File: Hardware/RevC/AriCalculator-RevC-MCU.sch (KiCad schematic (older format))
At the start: 13 parts, among them CON1 BDM, CON2 SPI, IC1 MC9S12G

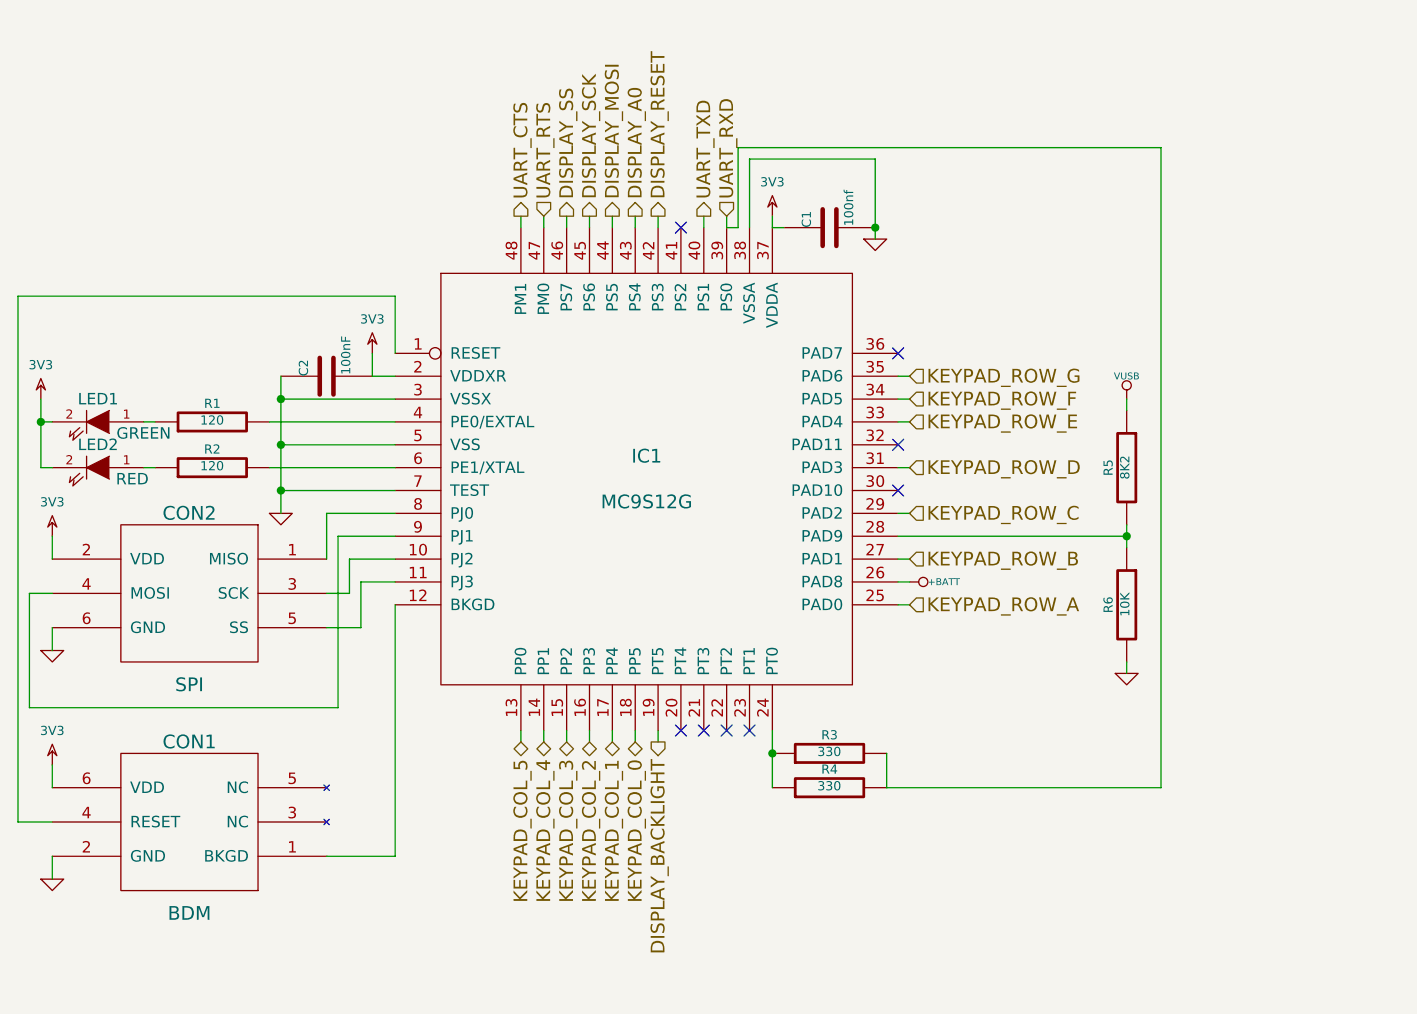
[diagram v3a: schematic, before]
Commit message: started RevC layout
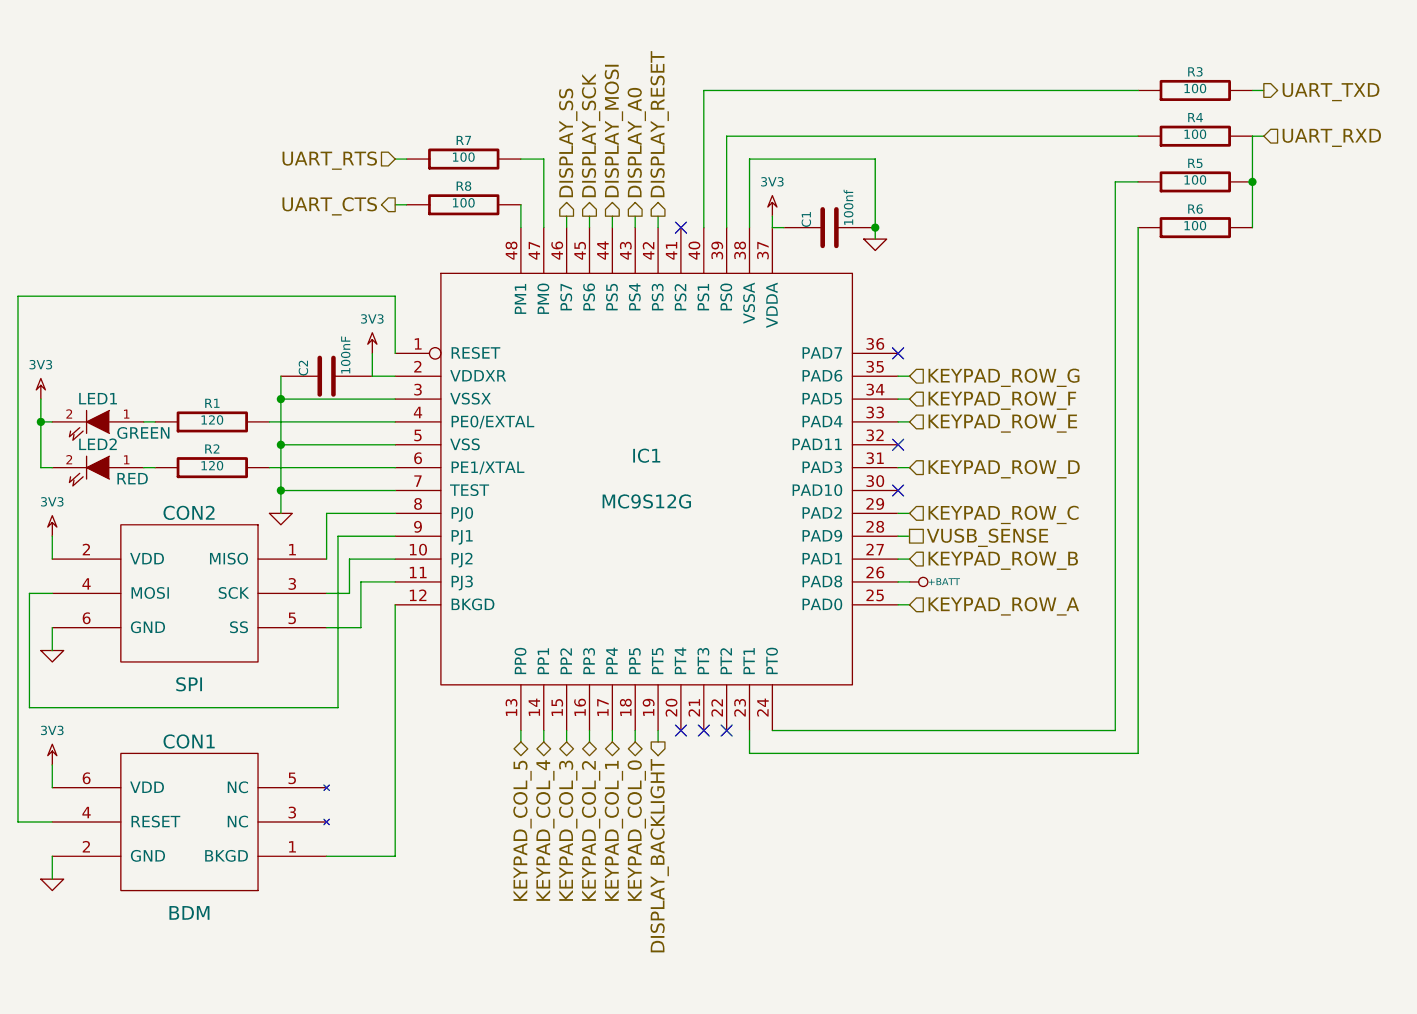
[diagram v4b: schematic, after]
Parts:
- added R7, R8: 100, ~, symbol R
- R3, R4: value 330 -> 100
- R5: value 8K2 -> 100
- R6: value 10K -> 100
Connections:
- net GND: no longer R6.2
- net UART_CTS: now also R8.1; no longer IC1.48 (PM1)
- net UART_RTS: now also R7.1; no longer IC1.47 (PM0)
- net UART_RXD: now also R5.2, R6.2; no longer IC1.39 (PS0), R3.2
- net UART_TXD: now also R3.2; no longer IC1.40 (PS1)
- net at IC1.23 (PT1): now also R6.1
- net VUSB: no longer names the net of R5.1
- net VUSB: now also IC1.24 (PT0)
- new net: IC1.39 (PS0), R4.1
- new net: IC1.40 (PS1), R3.1
- new net: IC1.47 (PM0), R7.2
- new net: IC1.48 (PM1), R8.2
- new net VUSB_SENSE: IC1.28 (PAD9)
- no-connect marks 8 -> 7
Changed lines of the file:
@@
 $EndComp
 $Comp
-L GND #PWR024
+L GND #PWR020
 U 1 1 544FF350
 P 4900 1400
-F 0 "#PWR024" H 4900 1400 30  0001 C CNN
+F 0 "#PWR020" H 4900 1400 30  0001 C CNN
 F 1 "GND" H 4900 1330 30  0001 C CNN
 F 2 "" H 4900 1400 60  0000 C CNN
@@
 $EndComp
 $Comp
-L GND #PWR025
+L GND #PWR021
 U 1 1 544FF410
 P 2300 2600
-F 0 "#PWR025" H 2300 2600 30  0001 C CNN
+F 0 "#PWR021" H 2300 2600 30  0001 C CNN
 F 1 "GND" H 2300 2530 30  0001 C CNN
 F 2 "" H 2300 2600 60  0000 C CNN
@@
 $EndComp
 $Comp
-L GND #PWR026
+L GND #PWR022
 U 1 1 544FF5A5
 P 1300 4200
-F 0 "#PWR026" H 1300 4200 30  0001 C CNN
+F 0 "#PWR022" H 1300 4200 30  0001 C CNN
 F 1 "GND" H 1300 4130 30  0001 C CNN
 F 2 "" H 1300 4200 60  0000 C CNN
@@
 $EndComp
 $Comp
-L GND #PWR027
+L GND #PWR023
 U 1 1 544FF75E
 P 1300 3200
-F 0 "#PWR027" H 1300 3200 30  0001 C CNN
+F 0 "#PWR023" H 1300 3200 30  0001 C CNN
 F 1 "GND" H 1300 3130 30  0001 C CNN
 F 2 "" H 1300 3200 60  0000 C CNN
@@
 	1    0    0    -1
 $EndComp
-$Comp
-L VUSB #PWR028
-U 1 1 54500312
-P 6000 2100
-F 0 "#PWR028" H 6000 2050 20  0001 C CNN
-F 1 "VUSB" H 6000 2200 30  0000 C CNN
-F 2 "" H 6000 2100 60  0000 C CNN
-F 3 "" H 6000 2100 60  0000 C CNN
-	1    6000 2100
-	1    0    0    -1
-$EndComp
-$Comp
-L R R5
-U 1 1 54500321
-P 6000 2400
-F 0 "R5" V 6080 2400 40  0000 C CNN
-F 1 "8K2" V 6007 2401 40  0000 C CNN
-F 2 "~" V 5930 2400 30  0000 C CNN
-F 3 "~" H 6000 2400 30  0000 C CNN
-	1    6000 2400
-	-1   0    0    -1
-$EndComp
-$Comp
-L R R6
-U 1 1 54500330
-P 6000 3000
-F 0 "R6" V 6080 3000 40  0000 C CNN
-F 1 "10K" V 6007 3001 40  0000 C CNN
-F 2 "~" V 5930 3000 30  0000 C CNN
-F 3 "~" H 6000 3000 30  0000 C CNN
-	1    6000 3000
-	-1   0    0    -1
-$EndComp
-$Comp
-L GND #PWR029
-U 1 1 5450033F
-P 6000 3300
-F 0 "#PWR029" H 6000 3300 30  0001 C CNN
-F 1 "GND" H 6000 3230 30  0001 C CNN
-F 2 "" H 6000 3300 60  0000 C CNN
-F 3 "" H 6000 3300 60  0000 C CNN
-	1    6000 3300
-	1    0    0    -1
-$EndComp
-$Comp
-L R R3
-U 1 1 5450048A
-P 4700 3650
-F 0 "R3" V 4780 3650 40  0000 C CNN
-F 1 "330" V 4707 3651 40  0000 C CNN
-F 2 "~" V 4630 3650 30  0000 C CNN
-F 3 "~" H 4700 3650 30  0000 C CNN
-	1    4700 3650
-	0    -1   -1   0
-$EndComp
-$Comp
-L R R4
-U 1 1 54500499
-P 4700 3800
-F 0 "R4" V 4780 3800 40  0000 C CNN
-F 1 "330" V 4707 3801 40  0000 C CNN
-F 2 "~" V 4630 3800 30  0000 C CNN
-F 3 "~" H 4700 3800 30  0000 C CNN
-	1    4700 3800
-	0    -1   -1   0
-$EndComp
 Text HLabel 3950 3600 3    60   Output ~ 0
 DISPLAY_BACKLIGHT
@@
 Connection ~ 1250 2200
 Wire Wire Line
-	6000 2100 6000 2150
-Wire Wire Line
-	6000 2650 6000 2750
-Connection ~ 6000 2700
-Wire Wire Line
-	6000 3250 6000 3300
-Wire Wire Line
-	4450 3550 4450 3800
-Connection ~ 4450 3650
-Wire Wire Line
-	4950 3650 4950 3800
-Wire Wire Line
-	4950 3800 6150 3800
-Wire Wire Line
-	6150 3800 6150 1000
-Wire Wire Line
 	3950 3550 3950 3600
-NoConn ~ 4350 3550
 NoConn ~ 4250 3550
 NoConn ~ 4150 3550
@@
 KEYPAD_ROW_F
 $Comp
-L +BATT #PWR030
+L +BATT #PWR024
 U 1 1 544FFB66
 P 5050 2900
-F 0 "#PWR030" H 5050 2850 20  0001 C CNN
+F 0 "#PWR024" H 5050 2850 20  0001 C CNN
 F 1 "+BATT" V 5050 3050 30  0000 C CNN
 F 2 "" H 5050 2900 60  0000 C CNN
@@
 Wire Wire Line
 	5000 2000 5050 2000
-Text HLabel 3350 1300 1    60   Output ~ 0
+Text HLabel 2800 1250 0    60   Output ~ 0
 UART_CTS
-Text HLabel 3450 1300 1    60   Input ~ 0
+Text HLabel 2800 1050 0    60   Input ~ 0
 UART_RTS
-Text HLabel 4150 1300 1    60   Output ~ 0
+Text HLabel 6600 750  2    60   Output ~ 0
 UART_TXD
-Text HLabel 4250 1300 1    60   Input ~ 0
+Text HLabel 6600 950  2    60   Input ~ 0
 UART_RXD
 Text HLabel 3550 1300 1    60   Output ~ 0
@@
 Connection ~ 4900 1350
 Wire Wire Line
-	4150 1300 4150 1350
-Wire Wire Line
 	3950 1300 3950 1350
 Wire Wire Line
@@
 Wire Wire Line
 	3550 1300 3550 1350
-Wire Wire Line
-	3450 1300 3450 1350
-Wire Wire Line
-	3350 1300 3350 1350
-Wire Wire Line
-	4250 1300 4250 1350
-Wire Wire Line
-	4250 1350 4300 1350
-Wire Wire Line
-	4300 1350 4300 1000
-Wire Wire Line
-	4300 1000 6150 1000
 $Comp
 L 3V3 #PWR32
@@
 Wire Wire Line
 	5050 2900 5000 2900
-Wire Wire Line
-	5000 2700 6000 2700
+Text HLabel 5050 2700 2    60   UnSpc ~ 0
+VUSB_SENSE
+Wire Wire Line
+	5050 2700 5000 2700
+$Comp
+L R R7
+U 1 1 545B39EE
+P 3100 1050
+F 0 "R7" V 3180 1050 40  0000 C CNN
+F 1 "100" V 3107 1051 40  0000 C CNN
+F 2 "~" V 3030 1050 30  0000 C CNN
+F 3 "~" H 3100 1050 30  0000 C CNN
+	1    3100 1050
+	0    -1   -1   0
+$EndComp
+$Comp
+L R R8
+U 1 1 545B39FD
+P 3100 1250
+F 0 "R8" V 3180 1250 40  0000 C CNN
+F 1 "100" V 3107 1251 40  0000 C CNN
+F 2 "~" V 3030 1250 30  0000 C CNN
+F 3 "~" H 3100 1250 30  0000 C CNN
+	1    3100 1250
+	0    -1   -1   0
+$EndComp
+$Comp
+L R R3
+U 1 1 545B3A0C
+P 6300 750
+F 0 "R3" V 6380 750 40  0000 C CNN
+F 1 "100" V 6307 751 40  0000 C CNN
+F 2 "~" V 6230 750 30  0000 C CNN
+F 3 "~" H 6300 750 30  0000 C CNN
+	1    6300 750
+	0    -1   -1   0
+$EndComp
+$Comp
+L R R5
+U 1 1 545B3A1B
+P 6300 1150
+F 0 "R5" V 6380 1150 40  0000 C CNN
+F 1 "100" V 6307 1151 40  0000 C CNN
+F 2 "~" V 6230 1150 30  0000 C CNN
+F 3 "~" H 6300 1150 30  0000 C CNN
+	1    6300 1150
+	0    -1   -1   0
+$EndComp
+$Comp
+L R R4
+U 1 1 545B3A2A
+P 6300 950
+F 0 "R4" V 6380 950 40  0000 C CNN
+F 1 "100" V 6307 951 40  0000 C CNN
+F 2 "~" V 6230 950 30  0000 C CNN
+F 3 "~" H 6300 950 30  0000 C CNN
+	1    6300 950
+	0    -1   -1   0
+$EndComp
+Wire Wire Line
+	3350 1350 3350 1250
+Wire Wire Line
+	3450 1350 3450 1050
+Wire Wire Line
+	3450 1050 3350 1050
+Wire Wire Line
+	2850 1050 2800 1050
+Wire Wire Line
+	2850 1250 2800 1250
+$Comp
+L R R6
+U 1 1 545B3C06
+P 6300 1350
+F 0 "R6" V 6380 1350 40  0000 C CNN
+F 1 "100" V 6307 1351 40  0000 C CNN
+F 2 "~" V 6230 1350 30  0000 C CNN
+F 3 "~" H 6300 1350 30  0000 C CNN
+	1    6300 1350
+	0    -1   -1   0
+$EndComp
+Wire Wire Line
+	4250 950  4250 1350
+Wire Wire Line
+	4250 950  6050 950
+Wire Wire Line
+	4150 1350 4150 750
+Wire Wire Line
+	4150 750  6050 750
+Wire Wire Line
+	6550 750  6600 750
+Wire Wire Line
+	6550 950  6600 950
+Wire Wire Line
+	6550 950  6550 1350
+Connection ~ 6550 1150
+Wire Wire Line
+	4450 3550 5950 3550
+Wire Wire Line
+	5950 3550 5950 1150
+Wire Wire Line
+	5950 1150 6050 1150
+Wire Wire Line
+	6050 1350 6050 3650
+Wire Wire Line
+	6050 3650 4350 3650
+Wire Wire Line
+	4350 3650 4350 3550
 $EndSCHEMATC
